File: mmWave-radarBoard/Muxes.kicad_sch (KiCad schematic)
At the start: 28 parts, among them U701 TS3A27518ERTW, U702 SN65LVDS047D, U703 SN65LVDS047D, U704 TS3A27518ERTW, U705 TS3A5017RGY, U706 TS3A5017RGY

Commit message: Updated schematic of the radar module
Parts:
- removed U705, U706: TS3A5017RGY, Package_DFN_QFN:Texas_RGY_R-PVQFN-N16_EP2.05x2.55mm, symbol Analog_Switch:TS3A5017RGY
- added C296: 0.1uF, symbol Device:C
- added R296, R297, R300, R306: 10k, symbol Device:R
- added R298, R299, R302, R305, R310: 0, symbol Device:R
- added R301, R309: 750, symbol Device:R
- added R303, R307: 82.5k, symbol Device:R
- added R304, R308: 7.87k, symbol Device:R
- added R311: 1k, symbol Device:R
- added SW701: SW_SPDT, symbol Switch:SW_SPDT
- added SW702: SW_DIP_x06, symbol Switch:SW_DIP_x06
- added SW703: SW_DIP_x04, symbol Switch:SW_DIP_x04
- added TP215: TestPoint, symbol Connector:TestPoint
- added U705, U708: TS3A5018RSVR, TS3A5018RSVR:QFN40P260X180X55-16N, symbol TS3A5018RSVR:TS3A5018RSVR
- added U706: TS3A44159PWR, TS3A44159PWR:SOP65P640X120-16N, symbol TS3A44159PWR:TS3A44159PWR
- R295: now not fitted
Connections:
- net DCA_FTDI_HOST_INTR_1: now also U705.9 (NC3)
- net DCA_FTDI_SPI_CLK: now also U705.1 (NO1)
- net DCA_FTDI_SPI_CS: now also U705.8 (NO3)
- net DCA_FTDI_SPI_MISO: now also U705.16 (NC1)
- net DCA_HOST_INTR_GPIO_0_LED: now also U705.10 (COM4)
- net DCA_SPI_CLK_I2C_SCL: now also U705.2 (COM1)
- net DCA_SPI_CS_I2C_SDA: now also U705.5 (COM2)
- net DCA_SPI_MISO_REG_MODE: now also U705.7 (COM3)
- net DCA_TCK: now also U708.1 (NO1)
- net DCA_TDI: now also U708.8 (NO3)
- net DCA_TDO: now also U708.16 (NC1)
- net DCA_TMS: now also U708.9 (NC3)
- net GND: now also C296.1, R303.1, R307.1, SW702.10, SW702.11, SW702.7, SW702.8, SW702.9, SW703.5, SW703.6, SW703.7, U705.6 (GND), U706.4 (GND), U708.6 (GND)
- net I2C_SCL: now also U705.4 (NO2)
- net I2C_SDA: now also U705.11 (NO4)
- net MUX_CTRL_FTDI_DCA_SPI: now also SW703.3
- net MUX_CTRL_LVDS_UART_CAN_TP: now also SW702.3
- net MUX_CTRL_SPI_I2C_MODE: now also SW702.6, U705.15 (IN)
- net MUX_CTRL_XDS_DCA_JTAG: now also SW702.2, U708.15 (IN)
- net REG_MODE_SELECT: now also U705.3 (NC2)
- net USER_LED_SW_GPIO_0: now also U705.12 (NC4)
- net VCC_3V3: now also C296.2, R296.1, R297.1, R304.2, R311.2, SW702.12, U705.14 (V+), U706.12 (VCC), U708.14 (V+)
- net XDS_DCA_TCK: now also U708.2 (COM1)
- net XDS_DCA_TDI: now also U708.5 (COM2)
- net XDS_DCA_TDO_SOP0: now also R300.1, U708.7 (COM3)
- net XDS_DCA_TMS: now also U708.10 (COM4)
- net XDS_TCK: now also U708.4 (NO2)
- net XDS_TDI: now also U708.11 (NO4)
- net XDS_TDO: now also U708.3 (NC2)
- net XDS_TMS: now also U708.12 (NC4)
- net XDS_UARTA_RX_CAN_RX: now also R298.1, U706.6 (COM3)
- net XDS_UARTA_TX_CAN_TX: now also R299.1, U706.10 (COM4)
- net at R290.2: now also U708.13 (~{EN})
- net at R292.2: now also U705.13 (~{EN})
- new net: R306.2, R307.2, R308.1, R309.1
- new net: R311.1, SW703.8
- new net: R300.2, R301.1, SW701.2 (B)
- new net CAN_PHY_RX: U706.5 (NO3)
- new net CAN_PHY_TX: U706.9 (NO4)
- new net CAN_STB_CTRL: SW703.1
- new net DCA_RS232_RX: U706.3 (NC2)
- new net DCA_RS232_TX: U706.15 (NC1)
- new net FTDI_DOP0: R301.2, R302.1
- new net FTDI_DOP1: R309.2, R310.1
- new net LIN_PHY_EN_CTRL: SW703.2
- new net MUX_CTRL_RS232: R296.2, SW702.4, U706.16 (IN1-2)
- new net MUX_CTRL_UARTA_CAN: R297.2, SW702.5, U706.8 (IN3-4)
- new net NET_SOP1: R308.2, SW702.1
- new net PMIC_CLKOUT: R305.1, TP215.1
- new net PMIC_CLKOUT_LIN_PHY_TX_SOP1: R305.2, R306.1
- new net SOP0_H: R304.1, SW701.1 (A)
- new net SOP0_L: R303.2, SW701.3 (C)
- new net XDS_DCA_RS232_RX: U706.2 (COM2)
- new net XDS_DCA_RS232_TX: U706.14 (COM1)
- new net XDS_RS232_RX: U706.1 (NO2)
- new net XDS_RS232_TX: U706.13 (NO1)
- new net XDS_SOP0: R302.2
- new net XDS_SOP1: R310.2
- new net XDS_UARTA_RX: R298.2, U706.7 (NC3)
- new net XDS_UARTA_TX: R299.2, U706.11 (NC4)
- no-connect marks 9 -> 10
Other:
- note removed: "TS3A44159PWR"
- note removed: "TS3A5018RSVR"
- moved on the sheet: C289, C290, C291, C292, C293, C294, C295, R287, R288, R289, R290, R291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

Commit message: Removed unnecessary bits
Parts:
- removed C288, C289, C291, C293, C294, C296: 0.1uF, symbol Device:C
- removed C290, C292: 10nF, symbol Device:C
- removed R285, R286, R288, R289, R291, R296, R297: 10k, symbol Device:R
- removed R287, R298, R299, R302, R310: 0, symbol Device:R
- removed R290: 4.7k, symbol Device:R
- removed SW702: SW_DIP_x06, symbol Switch:SW_DIP_x06
- removed TP212, TP213, TP214: TestPoint, symbol Connector:TestPoint
- removed U701, U704: TS3A27518ERTW, Package_DFN_QFN:WQFN-24-1EP_4x4mm_P0.5mm_EP2.6x2.6mm, symbol Analog_Switch:TS3A27518ERTW
- removed U702, U703: SN65LVDS047D, Package_SO:SOIC-16_3.9x9.9mm_P1.27mm, symbol Interface:SN65LVDS047D
- removed U706: TS3A44159PWR, TS3A44159PWR:SOP65P640X120-16N, symbol TS3A44159PWR:TS3A44159PWR
- removed U708: TS3A5018RSVR, TS3A5018RSVR:QFN40P260X180X55-16N, symbol TS3A5018RSVR:TS3A5018RSVR
- added C286, C287: 0.1uF, symbol Device:C
- added D502, D503: LED GREEN, symbol Device:LED
- added MOSFET501, MOSFET502: SSM3K35AMFV_L3F, symbol SSM3K35AMFV:SSM3K35AMFV_L3F
- added R272, R273: 10k, symbol Device:R
- added R274: 0, symbol Device:R
- added R275, R276, R277: 100k, symbol Device:R
- added R280: 4.7k, symbol Device:R
- added R281, R283: 510, symbol Device:R
- added R282: 2.2k, symbol Device:R
- added SW501, SW502: SW_DPST, symbol Switch:SW_DPST
- added U501: SN74LVC1G11DSFR, SN74LVC1G11DSFR:SON35P100X100X40-6N, symbol SN74LVC1G11DSFR:SN74LVC1G11DSFR
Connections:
- net DCA_FTDI_HOST_INTR_1 is gone; now on net FTDI_HOST_INTR_1: R294.2, R295.1, U705.9 (NC3)
- net DCA_FTDI_SPI_CLK is gone; now on net FTDI_SPI_CLK: U705.1 (NO1)
- net DCA_FTDI_SPI_CS is gone; now on net FTDI_SPI_CS: U705.8 (NO3)
- net DCA_FTDI_SPI_MISO is gone; now on net FTDI_SPI_MISO: U705.16 (NC1)
- net MUX_CTRL_FTDI_DCA_SPI is gone; now on net LIN_PHY_EN_CTRL: SW703.3
- net CAN_STB_CTRL: now also SW703.2; no longer SW703.1
- net GND: now also C286.2, C287.1, MOSFET501.2, MOSFET502.2, R273.1, R275.1, SW502.1, SW502.3, U501.2 (GND); no longer SW703.7
- net LIN_PHY_EN_CTRL: no longer SW703.2
- net MUX_CTRL_SPI_I2C_MODE: now also SW703.4
- net NET_SOP1: now also SW703.1
- net USER_LED_SW_GPIO_0: now also R274.1, R283.2
- net VCC_3V3: now also SW703.8, C286.1, R272.2, R276.2, R277.2, R282.2, U501.5 (VCC)
- net at R311.1: now also SW703.7; no longer SW703.8
- net DCA_HOST_INTR_GPIO_0_LED renamed HOST_INTR_GPIO_0_LED
- net DCA_SPI_CLK_I2C_SCL renamed SPI_CLK_I2C_SCL
- net DCA_SPI_CS_I2C_SDA renamed SPI_CS_I2C_SDA
- net DCA_SPI_MISO_REG_MODE renamed SPI_MISO_REG_MODE
- net XDS_DCA_TDO_SOP0 renamed TDO_SOP0
- new net: R276.1, SW501.1, SW501.3
- new net: R274.2, R275.2, SW501.2, SW501.4
- new net: MOSFET502.1, R283.1
- new net: D503.1 (K), MOSFET502.3
- new net: D503.2 (A), R282.1
- new net: MOSFET501.1, R281.1
- new net: R272.1, U501.1 (A)
- new net: D502.1 (K), MOSFET501.3
- new net: D502.2 (A), R280.1
- new net 5V_IN: R280.2
- new net RADAR_~{RST}_1: U501.3 (B)
- new net RADAR_~{RST}_2: C287.2, R273.2, R277.1, SW502.2, SW502.4, U501.6 (C)
- new net ~{RADAR_RST}: R281.2, U501.4 (Y)
- no-connect marks 10 -> 0
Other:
- note removed: "Design Note: 100 ohms Differential traces"
- moved on the sheet: C295, R292, R293, R294, R295, R300, R301, R303, R304, R305, R306, R307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

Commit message: Finished schematic
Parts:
- C601: renamed from C295; footprint (none) -> Capacitor_SMD:C_0402_1005Metric
- C602: renamed from C287; footprint (none) -> Capacitor_SMD:C_0603_1608Metric
- C603: renamed from C286; footprint (none) -> Capacitor_SMD:C_0402_1005Metric
- D601: renamed from D502; footprint (none) -> LED_SMD:LED_0603_1608Metric
- D602: renamed from D503; footprint (none) -> LED_SMD:LED_0603_1608Metric
- MOSFET601: renamed from MOSFET501; footprint (none) -> SSM3K35AMFV:VESM_TOS-L
- MOSFET602: renamed from MOSFET502; footprint (none) -> SSM3K35AMFV:VESM_TOS-L
- R601: renamed from R294; footprint (none) -> Resistor_SMD:R_0201_0603Metric
- R602: renamed from R280; footprint (none) -> Resistor_SMD:R_0603_1608Metric
- R603: renamed from R282; footprint (none) -> Resistor_SMD:R_0603_1608Metric
- R604: renamed from R295; footprint (none) -> Resistor_SMD:R_0201_0603Metric
- R605: renamed from R293; footprint (none) -> Resistor_SMD:R_0201_0603Metric
- R606: renamed from R281; footprint (none) -> Resistor_SMD:R_0603_1608Metric
- R607: renamed from R283; footprint (none) -> Resistor_SMD:R_0603_1608Metric
- R608: renamed from R292; footprint (none) -> Resistor_SMD:R_0201_0603Metric
- R609: renamed from R277; footprint (none) -> Resistor_SMD:R_0603_1608Metric
- R610: renamed from R276; footprint (none) -> Resistor_SMD:R_0603_1608Metric
- R611: renamed from R274; footprint (none) -> Resistor_SMD:R_0603_1608Metric
- R612: renamed from R301; footprint (none) -> Resistor_SMD:R_0603_1608Metric
- R613: renamed from R275; footprint (none) -> Resistor_SMD:R_0603_1608Metric
- R614: renamed from R304; footprint (none) -> Resistor_SMD:R_0603_1608Metric
- R615: renamed from R300; footprint (none) -> Resistor_SMD:R_0603_1608Metric
- R616: renamed from R303; footprint (none) -> Resistor_SMD:R_0603_1608Metric
- R617: renamed from R272; footprint (none) -> Resistor_SMD:R_0603_1608Metric
- R618: renamed from R305; footprint (none) -> Resistor_SMD:R_0603_1608Metric
- R619: renamed from R309; footprint (none) -> Resistor_SMD:R_0603_1608Metric
- R620: renamed from R273; footprint (none) -> Resistor_SMD:R_0603_1608Metric
- R621: renamed from R311; footprint (none) -> Resistor_SMD:R_0603_1608Metric
- R622: renamed from R306; footprint (none) -> Resistor_SMD:R_0603_1608Metric
- R623: renamed from R308; footprint (none) -> Resistor_SMD:R_0603_1608Metric
- R624: renamed from R307; footprint (none) -> Resistor_SMD:R_0603_1608Metric
- SW601: renamed from SW502; footprint (none) -> Button_Switch_SMD:SW_SPST_PTS647_Sx70
- SW602: renamed from SW501; footprint (none) -> Button_Switch_SMD:SW_SPST_PTS647_Sx70
- SW603: renamed from SW701; footprint (none) -> Button_Switch_SMD:Nidec_Copal_CAS-120A
- SW604: renamed from SW703; footprint (none) -> Button_Switch_SMD:SW_DIP_SPSTx04_Slide_6.7x11.72mm_W8.61mm_P2.54mm_LowProfile
- TP601: renamed from TP215; footprint (none) -> TestPoint:TestPoint_Pad_D1.0mm
- renumbered U705 to U601, U501 to U602
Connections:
- net FTDI_HOST_INTR_1: now also U601.12 (NC4); no longer U601.9 (NC3)
- net FTDI_SPI_CLK: now also U601.16 (NC1); no longer U601.1 (NO1)
- net FTDI_SPI_CS: now also U601.3 (NC2); no longer U601.8 (NO3)
- net FTDI_SPI_MISO: now also U601.9 (NC3); no longer U601.16 (NC1)
- net I2C_SCL: now also U601.1 (NO1); no longer U601.4 (NO2)
- net I2C_SDA: now also U601.4 (NO2); no longer U601.11 (NO4)
- net REG_MODE_SELECT: now also U601.8 (NO3); no longer U601.3 (NC2)
- net USER_LED_SW_GPIO_0: now also U601.11 (NO4); no longer U601.12 (NC4)

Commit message: Updated radar PCB and schematic
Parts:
- R606, R607: footprint Resistor_SMD:R_0603_1608Metric -> Resistor_SMD:R_0402_1005Metric
- R617, R620: footprint Resistor_SMD:R_0603_1608Metric -> Resistor_SMD:R_0201_0603Metric

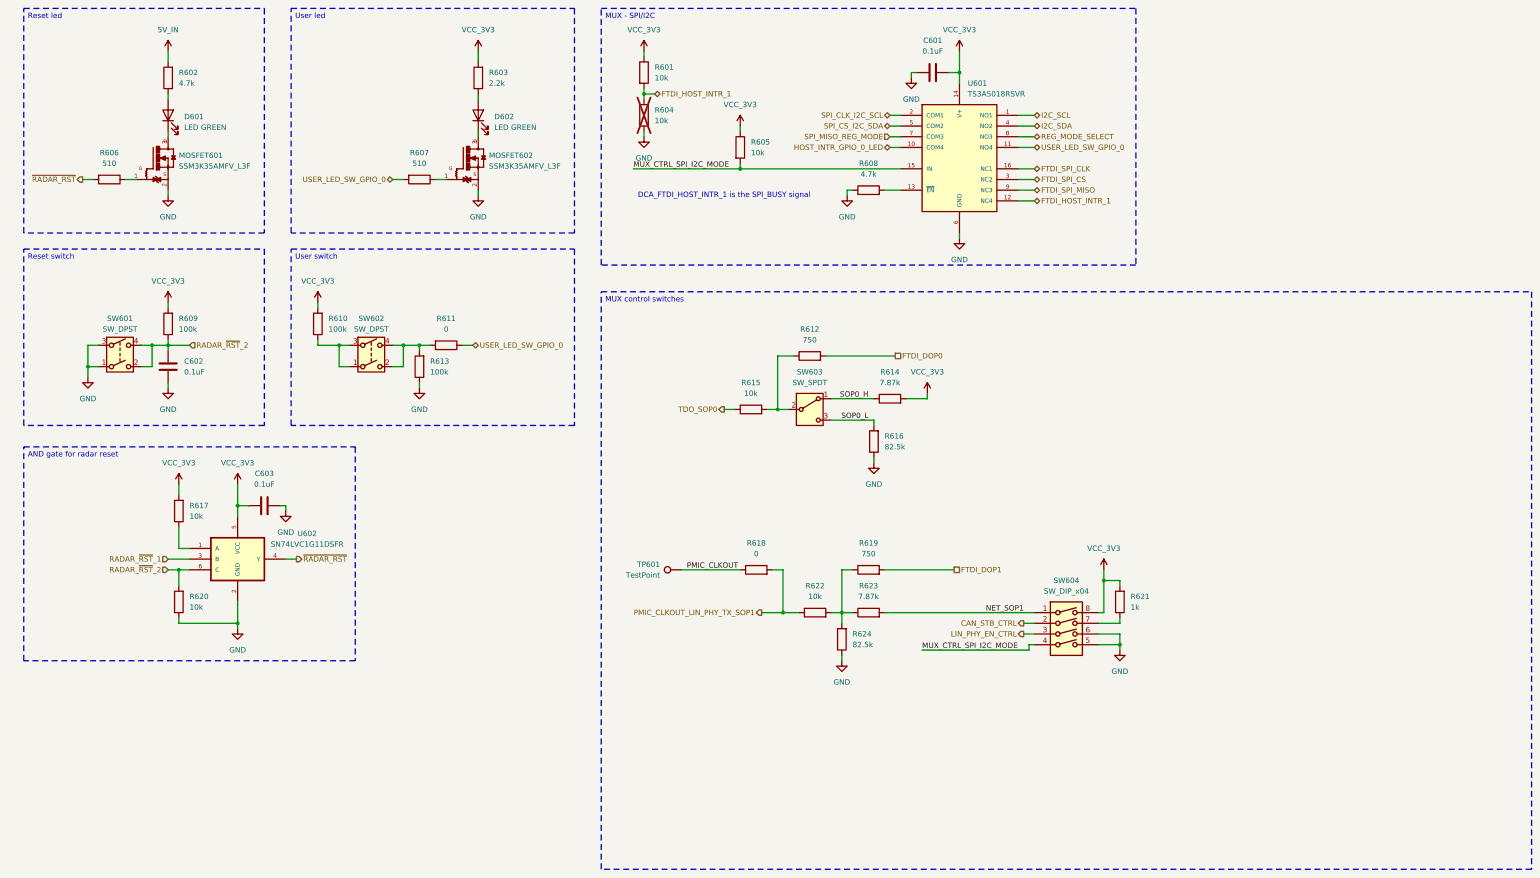
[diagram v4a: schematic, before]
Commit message: Updated schematic and PCB
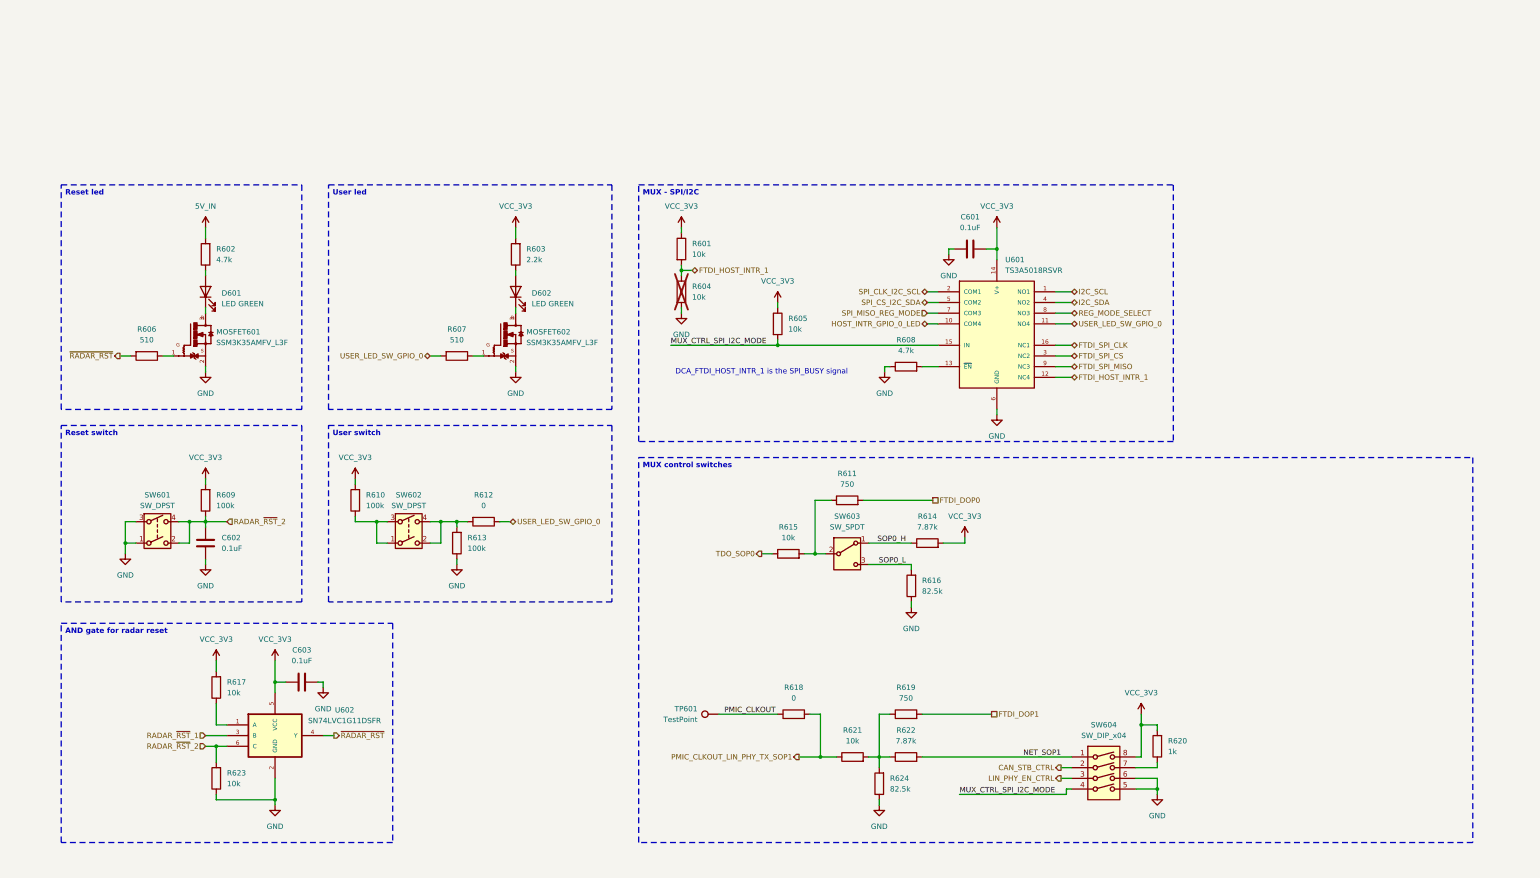
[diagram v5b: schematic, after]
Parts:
- renumbered R612 to R611, R611 to R612, R621 to R620, R622 to R621, R623 to R622, R620 to R623
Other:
- moved on the sheet: C601, C602, C603, D601, D602, MOSFET601, MOSFET602, R601, R602, R603, R604, R605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

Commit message: Updated PCB and schematic
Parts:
- SW601, SW602: footprint Button_Switch_SMD:SW_SPST_PTS647_Sx70 -> Button_Switch_SMD:SW_SPST_PTS810

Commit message: Updated PCB
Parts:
- R601, R604, R605, R608, R617, R623: footprint Resistor_SMD:R_0201_0603Metric -> Resistor_SMD:R_0402_1005Metric
